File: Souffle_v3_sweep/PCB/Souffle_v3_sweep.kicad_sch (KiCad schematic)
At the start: 82 parts, among them J1 LED, J2 4PIN, J3 OLED, SW1 SW_PUSH, SW10 SW_PUSH, SW11 SW_PUSH, SW12 SW_PUSH, SW13 SW_PUSH, SW14 SW_PUSH, SW15 SW_PUSH, SW16 SW_PUSH, SW17 SW_PUSH, SW18 SW_PUSH, SW19 SW_PUSH, SW2 SW_PUSH, SW20 SW_PUSH, SW21 SW_PUSH, SW22 SW_PUSH, SW23 SW_PUSH, SW24 SW_PUSH, SW25 SW_PUSH, SW25b1 RotaryEncoder_Switch, SW26 SW_PUSH, SW27 SW_PUSH, SW28 SW_PUSH, SW29 SW_PUSH, SW3 SW_PUSH, SW30 SW_PUSH, SW31 SW_SPDT, SW4 SW_PUSH, SW5 SW_PUSH, SW6 SW_PUSH, SW7 SW_PUSH, SW8 SW_PUSH, SW9 SW_PUSH, U1 ProMicro

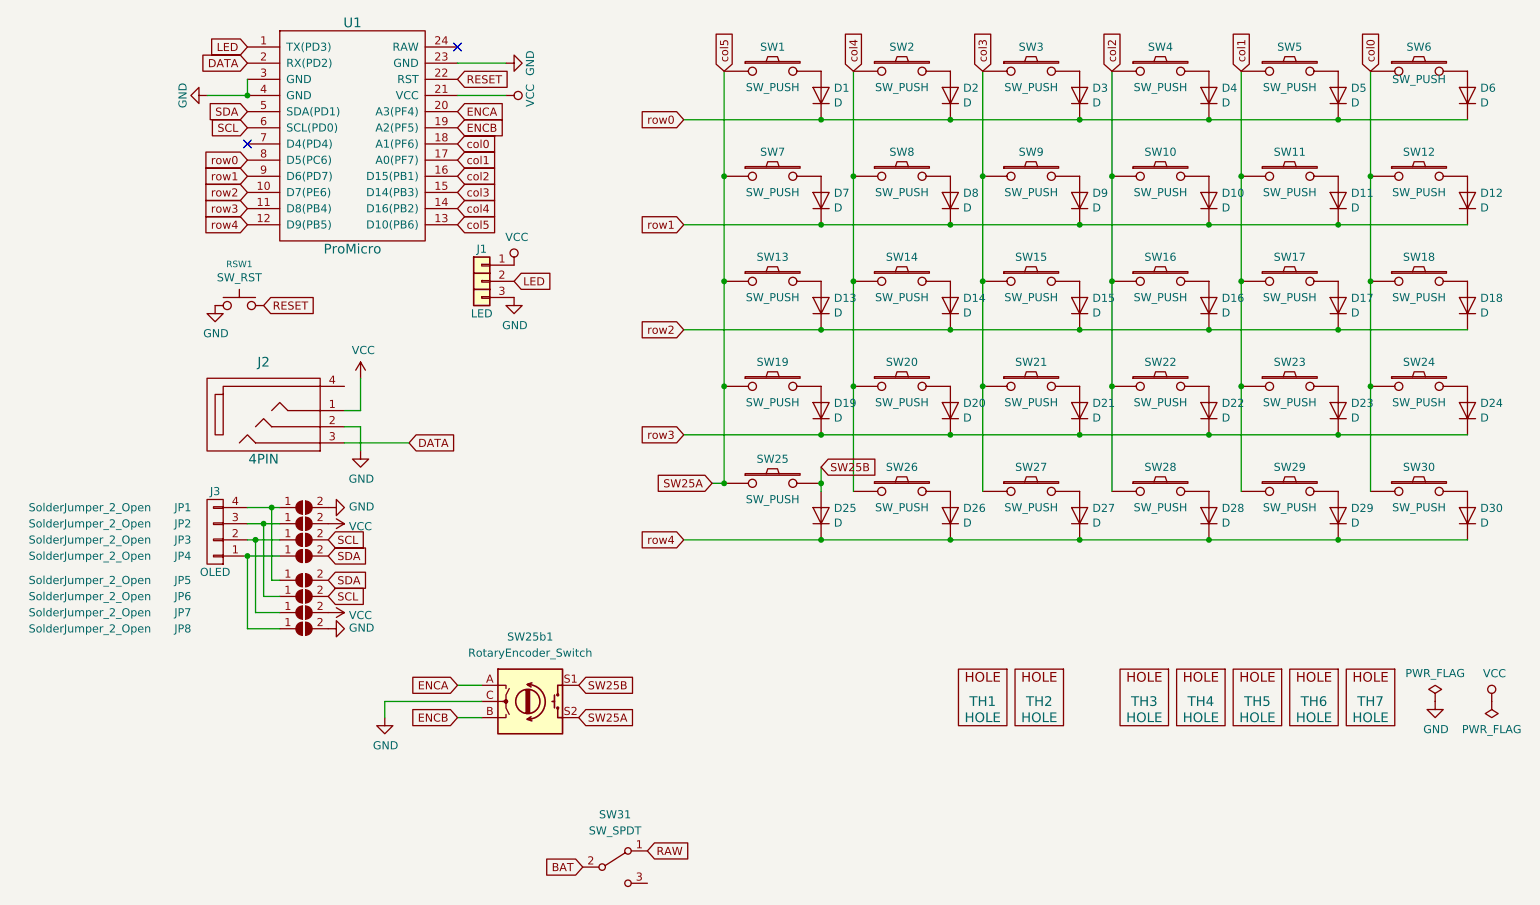
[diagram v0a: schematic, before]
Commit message: Added battery pins and power switch for nice!nano option.
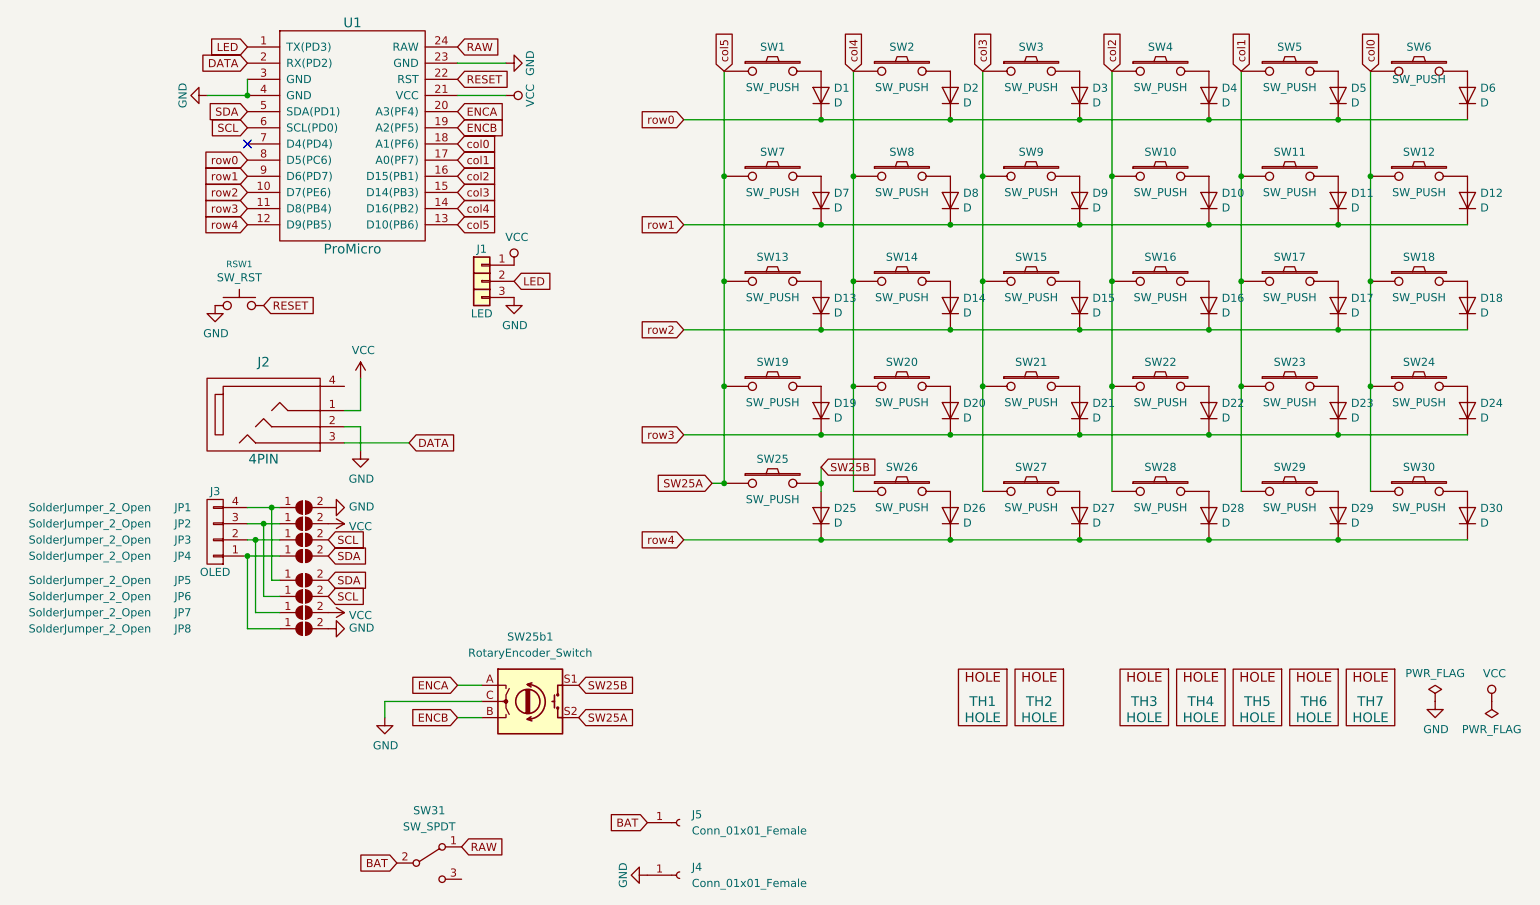
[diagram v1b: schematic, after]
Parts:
- added J4, J5: Conn_01x01_Female, Connector_PinSocket_2.00mm:PinSocket_1x01_P2.00mm_Vertical, symbol Connector:Conn_01x01_Female
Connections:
- net BAT: now also J5.1 (Pin_1)
- net GND: now also J4.1 (Pin_1)
- net RAW: now also U1.24 (RAW)
- no-connect marks 2 -> 1
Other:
- moved on the sheet: SW31
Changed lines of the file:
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@@
   )
   (no_connect (at 59.69 49.53))
-  (no_connect (at 92.71 34.29))
   (wire (pts (xy 59.69 109.22) (xy 62.23 109.22))
     (stroke (width 0) (type default) (color 0 0 0 0))
@@
     )
   )
-  (global_label "RAW" (shape input) (at 122.555 160.655 0) (fields_autoplaced)
-    (effects (font (size 1.27 1.27)) (justify left))
-    (property "Intersheet References" "${INTERSHEET_REFS}" (id 0) (at 128.7781 160.7344 0)
+  (global_label "SW25A" (shape input) (at 111.76 139.7 0) (fields_autoplaced)
+    (effects (font (size 1.27 1.27)) (justify left))
+    (property "Intersheet References" "${INTERSHEET_REFS}" (id 0) (at -12.7 -13.97 0)
+      (effects (font (size 1.27 1.27)) hide)
+    )
+  )
+  (global_label "col4" (shape input) (at 92.71 59.69 0) (fields_autoplaced)
+    (effects (font (size 1.27 1.27)) (justify left))
+    (property "Intersheet References" "${INTERSHEET_REFS}" (id 0) (at -5.08 -19.05 0)
+      (effects (font (size 1.27 1.27)) hide)
+    )
+  )
+  (global_label "RESET" (shape input) (at 62.23 74.93 0) (fields_autoplaced)
+    (effects (font (size 1.27 1.27)) (justify left))
+    (property "Intersheet References" "${INTERSHEET_REFS}" (id 0) (at -5.08 -19.05 0)
+      (effects (font (size 1.27 1.27)) hide)
+    )
+  )
+  (global_label "LED" (shape input) (at 101.6 71.12 0) (fields_autoplaced)
+    (effects (font (size 1.27 1.27)) (justify left))
+    (property "Intersheet References" "${INTERSHEET_REFS}" (id 0) (at -5.08 -19.05 0)
+      (effects (font (size 1.27 1.27)) hide)
+    )
+  )
+  (global_label "RAW" (shape input) (at 93.345 160.02 0) (fields_autoplaced)
+    (effects (font (size 1.27 1.27)) (justify left))
+    (property "Intersheet References" "${INTERSHEET_REFS}" (id 0) (at 99.5681 159.9406 0)
       (effects (font (size 1.27 1.27)) (justify left) hide)
-    )
-  )
-  (global_label "SW25A" (shape input) (at 111.76 139.7 0) (fields_autoplaced)
-    (effects (font (size 1.27 1.27)) (justify left))
-    (property "Intersheet References" "${INTERSHEET_REFS}" (id 0) (at -12.7 -13.97 0)
-      (effects (font (size 1.27 1.27)) hide)
-    )
-  )
-  (global_label "col4" (shape input) (at 92.71 59.69 0) (fields_autoplaced)
-    (effects (font (size 1.27 1.27)) (justify left))
-    (property "Intersheet References" "${INTERSHEET_REFS}" (id 0) (at -5.08 -19.05 0)
-      (effects (font (size 1.27 1.27)) hide)
-    )
-  )
-  (global_label "RESET" (shape input) (at 62.23 74.93 0) (fields_autoplaced)
-    (effects (font (size 1.27 1.27)) (justify left))
-    (property "Intersheet References" "${INTERSHEET_REFS}" (id 0) (at -5.08 -19.05 0)
-      (effects (font (size 1.27 1.27)) hide)
-    )
-  )
-  (global_label "LED" (shape input) (at 101.6 71.12 0) (fields_autoplaced)
-    (effects (font (size 1.27 1.27)) (justify left))
-    (property "Intersheet References" "${INTERSHEET_REFS}" (id 0) (at -5.08 -19.05 0)
-      (effects (font (size 1.27 1.27)) hide)
     )
   )
@@
     )
   )
-  (global_label "BAT" (shape input) (at 112.395 163.195 180) (fields_autoplaced)
+  (global_label "BAT" (shape input) (at 83.185 162.56 180) (fields_autoplaced)
     (effects (font (size 1.27 1.27)) (justify right))
-    (property "Intersheet References" "${INTERSHEET_REFS}" (id 0) (at 106.6557 163.2744 0)
+    (property "Intersheet References" "${INTERSHEET_REFS}" (id 0) (at 77.4457 162.6394 0)
       (effects (font (size 1.27 1.27)) (justify right) hide)
     )
@@
     )
   )
+  (global_label "RAW" (shape input) (at 92.71 34.29 0) (fields_autoplaced)
+    (effects (font (size 1.27 1.27)) (justify left))
+    (property "Intersheet References" "${INTERSHEET_REFS}" (id 0) (at 98.9331 34.2106 0)
+      (effects (font (size 1.27 1.27)) (justify left) hide)
+    )
+  )
   (global_label "SW25B" (shape input) (at 149.86 100.33 0) (fields_autoplaced)
     (effects (font (size 1.27 1.27)) (justify left))
@@
     (property "Intersheet References" "${INTERSHEET_REFS}" (id 0) (at -5.08 -19.05 0)
       (effects (font (size 1.27 1.27)) hide)
+    )
+  )
+  (global_label "BAT" (shape input) (at 122.555 156.21 180) (fields_autoplaced)
+    (effects (font (size 1.27 1.27)) (justify right))
+    (property "Intersheet References" "${INTERSHEET_REFS}" (id 0) (at 116.8157 156.2894 0)
+      (effects (font (size 1.27 1.27)) (justify right) hide)
     )
   )
@@
     )
   )
+  (symbol (lib_id "Connector:Conn_01x01_Female") (at 127.635 164.465 0) (unit 1)
+    (in_bom yes) (on_board yes) (fields_autoplaced)
+    (property "Reference" "J4" (id 0) (at 129.54 163.1949 0)
+      (effects (font (size 1.27 1.27)) (justify left))
+    )
+    (property "Value" "Conn_01x01_Female" (id 1) (at 129.54 165.7349 0)
+      (effects (font (size 1.27 1.27)) (justify left))
+    )
+    (property "Footprint" "Connector_PinSocket_2.00mm:PinSocket_1x01_P2.00mm_Vertical" (id 2) (at 127.635 164.465 0)
+      (effects (font (size 1.27 1.27)) hide)
+    )
+    (property "Datasheet" "~" (id 3) (at 127.635 164.465 0)
+      (effects (font (size 1.27 1.27)) hide)
+    )
+    (pin "1")
+  )
+  (symbol (lib_id "Connector:Conn_01x01_Female") (at 127.635 156.21 0) (unit 1)
+    (in_bom yes) (on_board yes) (fields_autoplaced)
+    (property "Reference" "J5" (id 0) (at 129.54 154.9399 0)
+      (effects (font (size 1.27 1.27)) (justify left))
+    )
+    (property "Value" "Conn_01x01_Female" (id 1) (at 129.54 157.4799 0)
+      (effects (font (size 1.27 1.27)) (justify left))
+    )
+    (property "Footprint" "Connector_PinSocket_2.00mm:PinSocket_1x01_P2.00mm_Vertical" (id 2) (at 127.635 156.21 0)
+      (effects (font (size 1.27 1.27)) hide)
+    )
+    (property "Datasheet" "~" (id 3) (at 127.635 156.21 0)
+      (effects (font (size 1.27 1.27)) hide)
+    )
+    (pin "1")
+  )
   (symbol (lib_id "power:GND") (at 77.47 97.79 0) (unit 1)
     (in_bom yes) (on_board yes)
@@
     (pin "1")
     (pin "2")
+  )
+  (symbol (lib_id "SofleKeyboard-rescue:GND-Lily58-cache-Lily58_Pro-rescue") (at 122.555 164.465 270) (unit 1)
+    (in_bom yes) (on_board yes)
+    (property "Reference" "#PWR0117" (id 0) (at 116.205 164.465 0)
+      (effects (font (size 1.27 1.27)) hide)
+    )
+    (property "Value" "GND" (id 1) (at 118.745 164.465 0))
+    (property "Footprint" "" (id 2) (at 122.555 164.465 0)
+      (effects (font (size 1.27 1.27)) hide)
+    )
+    (property "Datasheet" "" (id 3) (at 122.555 164.465 0)
+      (effects (font (size 1.27 1.27)) hide)
+    )
+    (pin "1")
   )
   (symbol (lib_id "SofleKeyboard-rescue:D-Lily58-cache-Lily58_Pro-rescue") (at 251.46 58.42 90) (unit 1)
@@
     (pin "2")
   )
-  (symbol (lib_id "Switch:SW_SPDT") (at 117.475 163.195 0) (unit 1)
+  (symbol (lib_id "Switch:SW_SPDT") (at 88.265 162.56 0) (unit 1)
     (in_bom yes) (on_board yes) (fields_autoplaced)
-    (property "Reference" "SW31" (id 0) (at 117.475 154.94 0))
-    (property "Value" "SW_SPDT" (id 1) (at 117.475 157.48 0))
-    (property "Footprint" "keebs:Switch_MSK-12C01-07" (id 2) (at 117.475 163.195 0)
-      (effects (font (size 1.27 1.27)) hide)
-    )
-    (property "Datasheet" "~" (id 3) (at 117.475 163.195 0)
+    (property "Reference" "SW31" (id 0) (at 88.265 154.305 0))
+    (property "Value" "SW_SPDT" (id 1) (at 88.265 156.845 0))
+    (property "Footprint" "keebs:Switch_MSK-12C01-07" (id 2) (at 88.265 162.56 0)
+      (effects (font (size 1.27 1.27)) hide)
+    )
+    (property "Datasheet" "~" (id 3) (at 88.265 162.56 0)
       (effects (font (size 1.27 1.27)) hide)
     )
@@
       (reference "#PWR0115") (unit 1) (value "VCC") (footprint "")
     )
+    (path "/77468f8d-8b79-4933-9447-fceda987fba3"
+      (reference "#PWR0117") (unit 1) (value "GND") (footprint "")
+    )
     (path "/b7935af4-92e9-4636-9f41-c8a2f872b07e"
       (reference "D1") (unit 1) (value "D") (footprint "SofleKeyboard-footprint:Diode_SOD123")
@@
       (reference "J3") (unit 1) (value "OLED") (footprint "SofleKeyboard-footprint:OLED_4Pin")
     )
+    (path "/60d3001b-ad5d-4287-9ca0-4cb5cf344d12"
+      (reference "J4") (unit 1) (value "Conn_01x01_Female") (footprint "Connector_PinSocket_2.00mm:PinSocket_1x01_P2.00mm_Vertical")
+    )
+    (path "/60f6be00-246d-4008-904f-c04a774a5981"
+      (reference "J5") (unit 1) (value "Conn_01x01_Female") (footprint "Connector_PinSocket_2.00mm:PinSocket_1x01_P2.00mm_Vertical")
+    )
     (path "/ad368f1f-7f07-41ad-8a98-e30f05bf3b99"

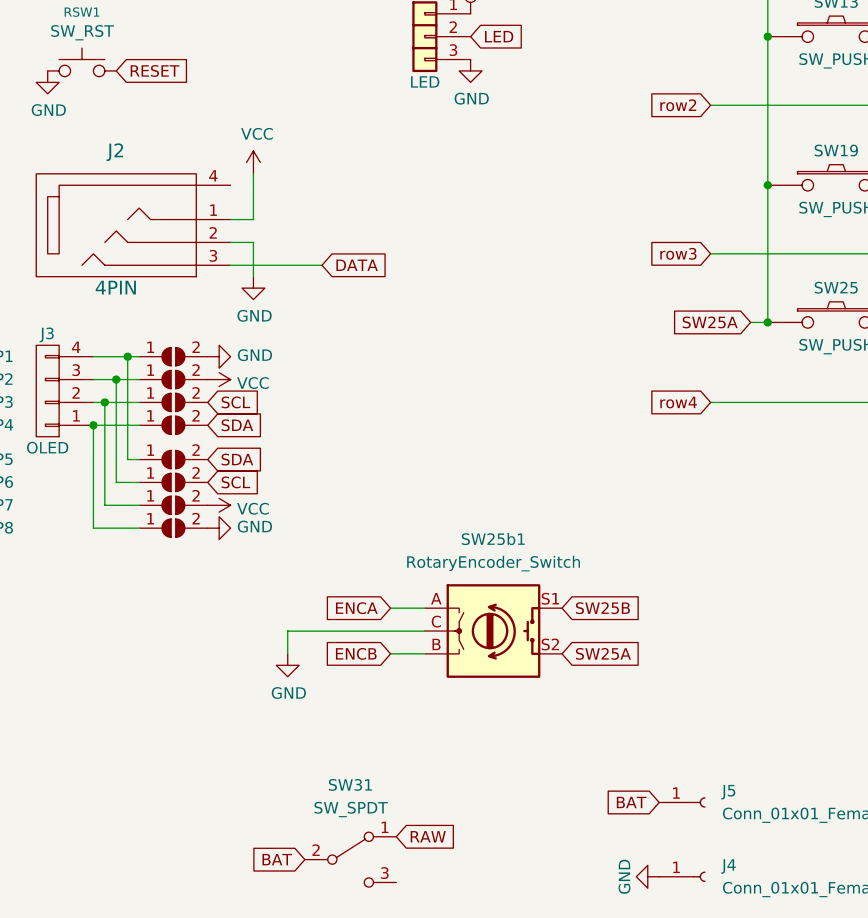
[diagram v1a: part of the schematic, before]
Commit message: Updated OLED connection to accomodate for NiceView option.
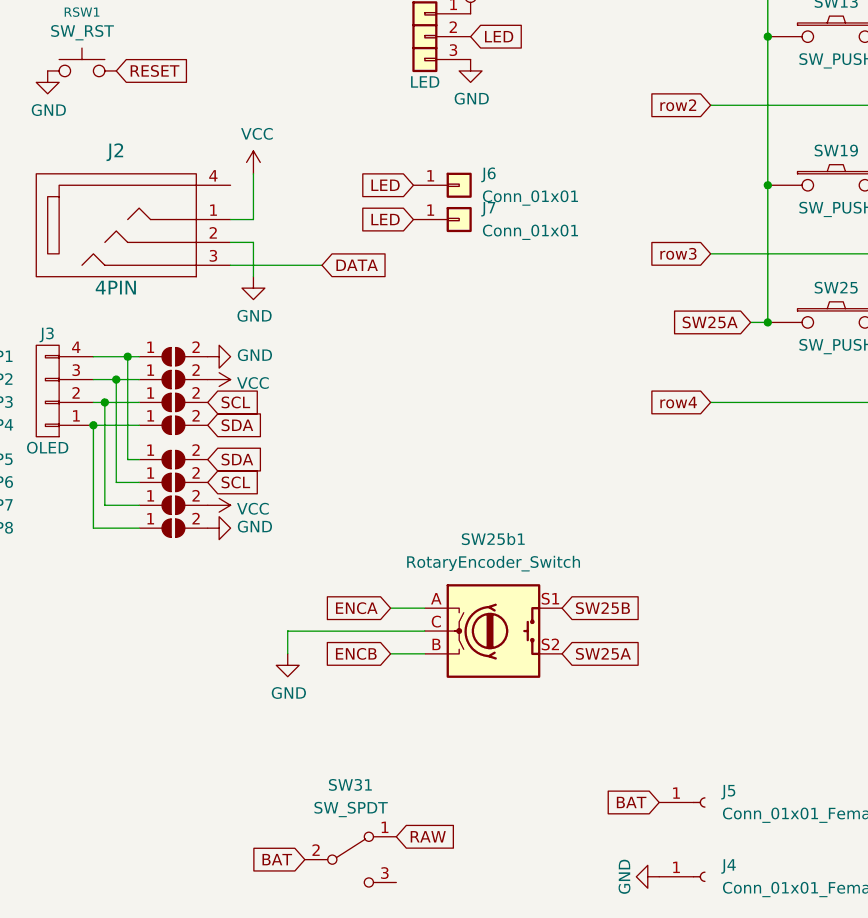
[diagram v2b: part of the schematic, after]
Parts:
- added J6, J7: Conn_01x01, Connector_PinSocket_2.00mm:PinSocket_1x01_P2.00mm_Vertical, symbol Connector_Generic:Conn_01x01
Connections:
- net LED: now also J6.1 (Pin_1), J7.1 (Pin_1)
